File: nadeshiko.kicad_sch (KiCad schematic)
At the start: 17 parts, among them SW1 SW_SP3T, U1 OPA2196xD, U2 OPA2196xD, U3 OPA2196xD

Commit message: Schema v2
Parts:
- removed U3: OPA2196xD, Package_SO:SOIC-8_3.9x4.9mm_P1.27mm, symbol Amplifier_Operational:OPA2196xD
- added D1, D2: 1N47xxA, Diode_THT:D_DO-41_SOD81_P10.16mm_Horizontal, symbol Diode:1N47xxA
- added R7: 1k, symbol Device:R
- added U3: TLV171, 4ms_Package_SOT:TSOT-23-5, symbol PCM_4ms_IC:TLV171
- C4: value 22nF -> 47nF
- R6: value 10k -> 8k
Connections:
- net +5V is gone; now on net GND: U1.3 (+)
- net +12V: now also R7.1, U3.5 (V+)
- net GND: now also U2.5 (+), U3.2 (V-), U3.4 (-)
- net OUT: now also U2.7
- net at C3.1, RV3.2, RV3.3: now also R1.1, SW1.1, U3.3 (+); no longer U2.5 (+)
- net at R2.2, R3.1, U1.1: now also D1.2 (A), D2.1 (K)
- net at RV1.1, RV1.2, SW1.2: now also R7.2, U3.1
- net at C4.1, R6.2: now also U2.6 (-)
- net at R1.2, R2.1, U1.2 (-): now also D1.1 (K), D2.2 (A)
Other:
- moved on the sheet: R2, U2B

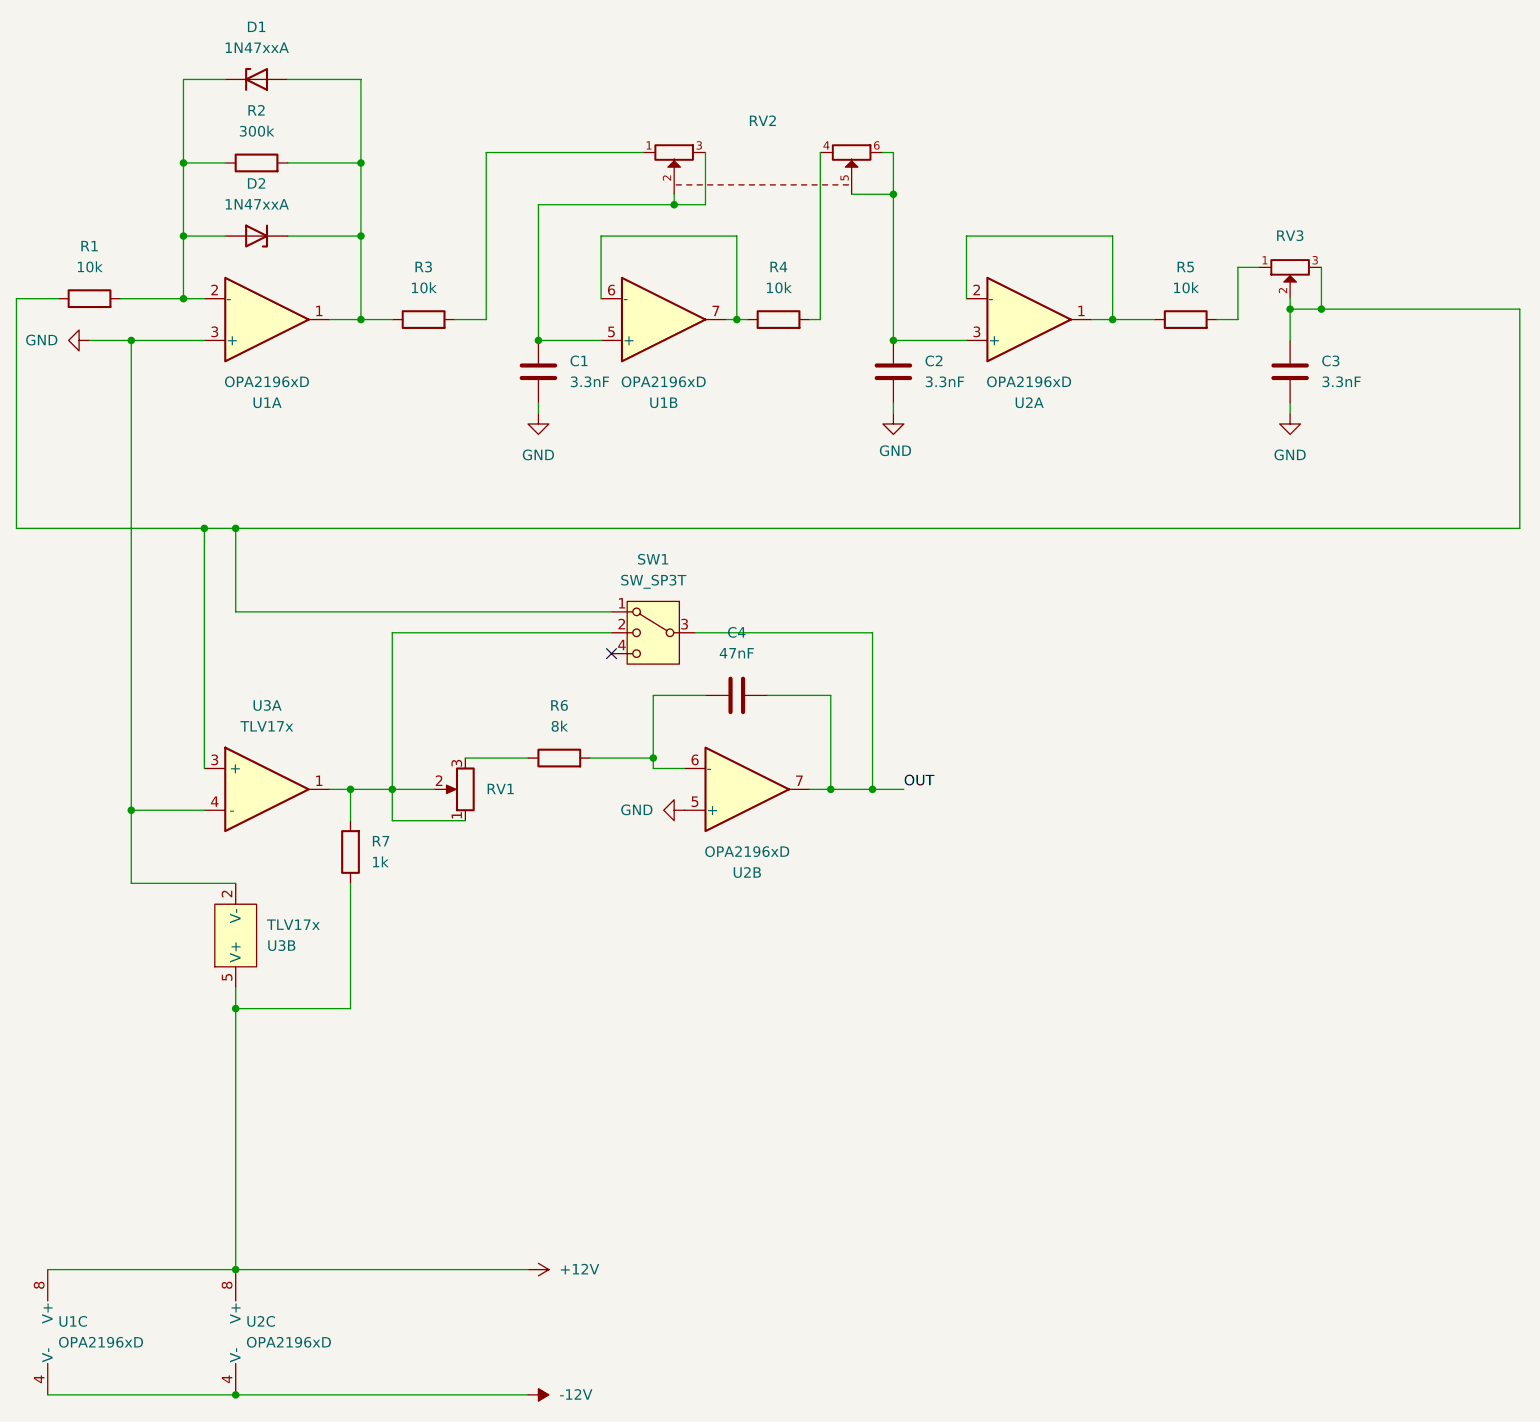
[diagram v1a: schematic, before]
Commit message: Schema v2a & custom footprint
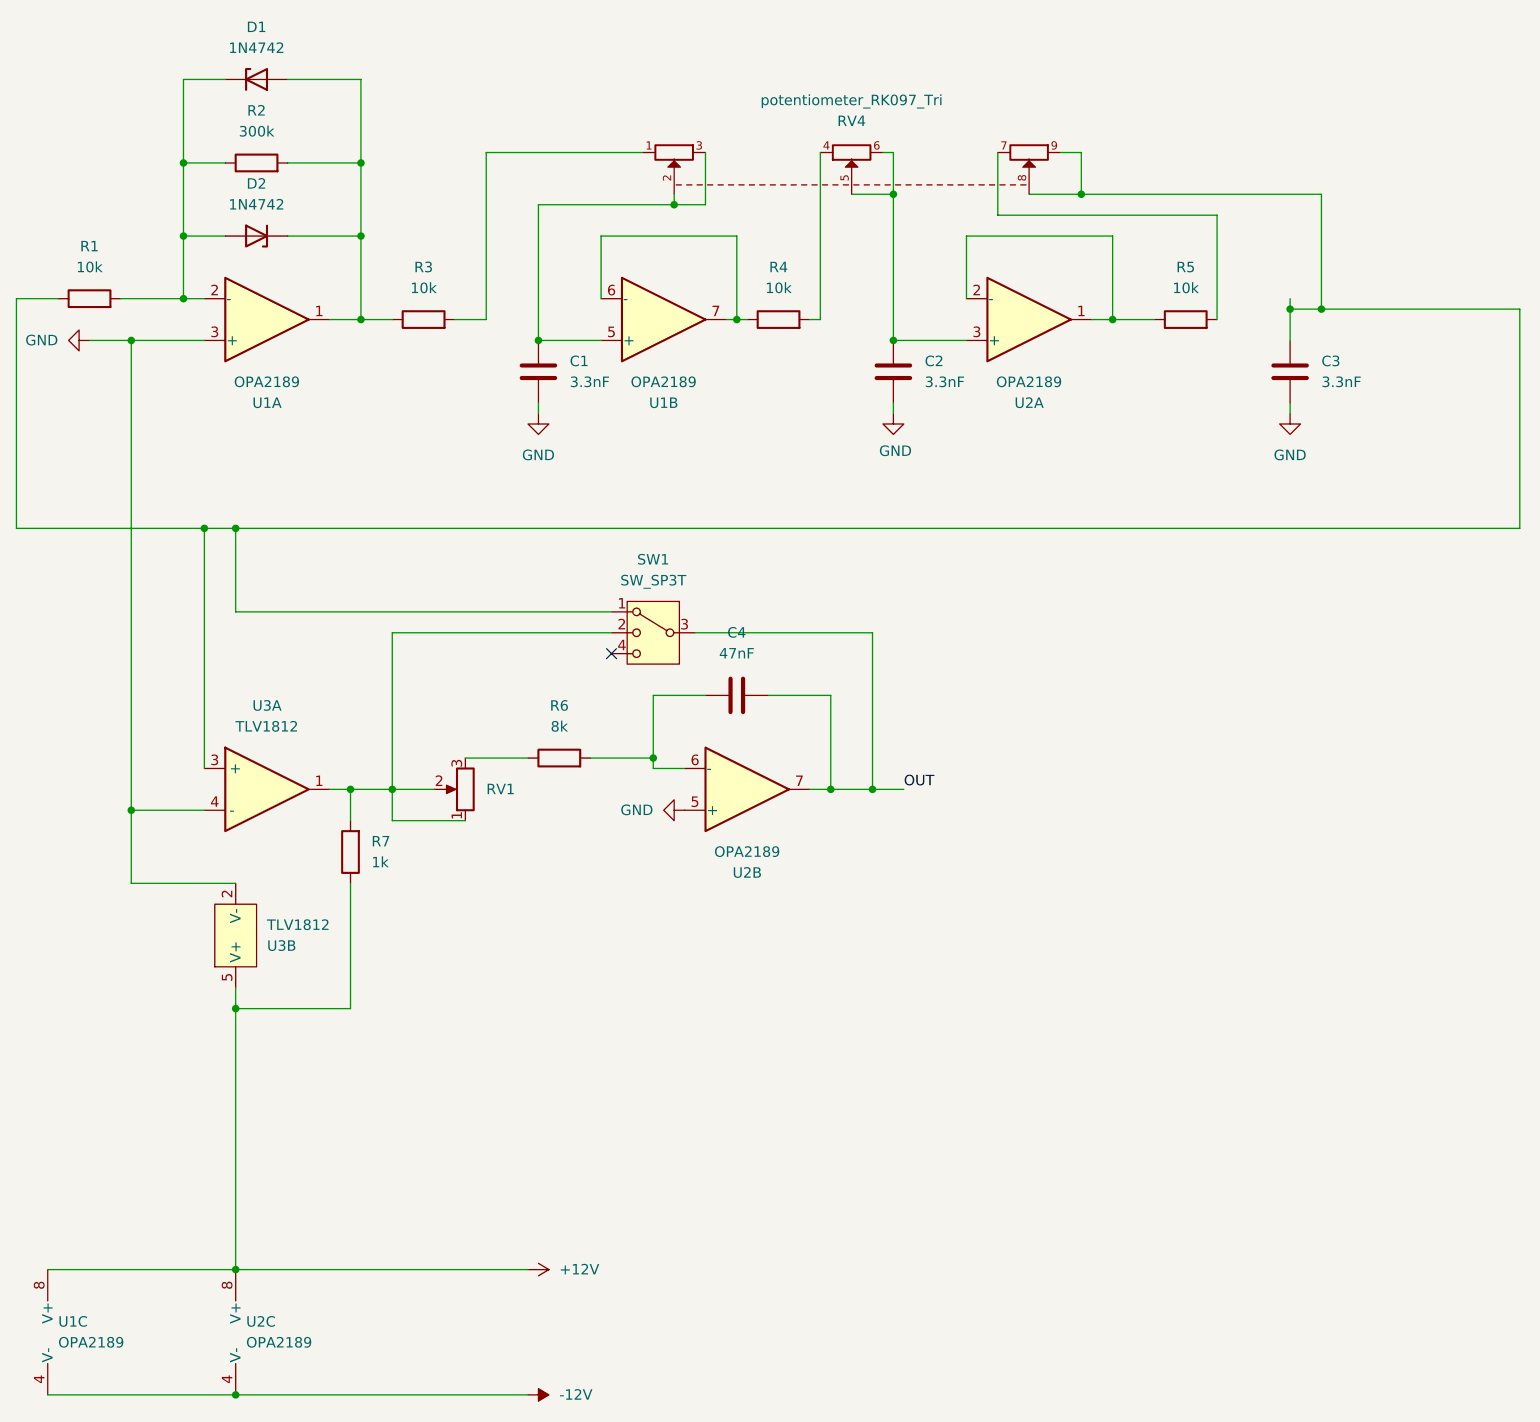
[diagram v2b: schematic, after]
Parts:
- removed RV2: potentiometer_RK163_Dual, Potentiometer_THT:Potentiometer_Alps_RK163_Dual_Horizontal, symbol PCM_SL_Devices:potentiometer_RK163_Dual
- removed RV3: potentiometer_RK163, Potentiometer_THT:Potentiometer_Alps_RK163_Single_Horizontal, symbol PCM_SL_Devices:potentiometer_RK163
- added RV4: potentiometer_RK097_Tri, Potentiometer_THT:Potentiometer_Alps_RK097_Tri_Horizontal, symbol PCM_SL_Devices:potentiometer_RK097_Tri
- C1, C2, C3, C4: footprint (none) -> Capacitor_SMD:C_0805_2012Metric_Pad1.18x1.45mm_HandSolder
- D1, D2: value 1N47xxA -> 1N4742
- R1, R2, R3, R4, R5, R6, R7: footprint (none) -> Resistor_SMD:R_0805_2012Metric_Pad1.20x1.40mm_HandSolder
- SW1: footprint (none) -> Button_Switch_SMD:SW_DIP_SPSTx02_Slide_9.78x7.26mm_W8.61mm_P2.54mm
- U1, U2: value OPA2196xD -> OPA2189
- U3: value TLV171 -> TLV1812; footprint 4ms_Package_SOT:TSOT-23-5 -> Package_TO_SOT_SMD:SOT-23-5_HandSoldering; Display TLV17x -> TLV1812
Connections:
- net at R5.2: now also RV4.7
- net at C3.1, R1.1, SW1.1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: now also RV4.8, RV4.9
- net at R3.2: now also RV4.1
- net at C2.1, U2.3 (+): now also RV4.5, RV4.6
- net at C1.1, U1.5 (+): now also RV4.2, RV4.3
- net at R4.2: now also RV4.4
